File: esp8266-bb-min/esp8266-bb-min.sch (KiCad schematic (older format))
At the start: 22 parts, among them J1 Conn_01x02_Male, J2 Conn_01x04_Male, J3 Conn_01x04_Male, J4 Conn_01x06_Male, J5 Conn_01x04_Male, J6 Conn_01x04_Male, J7 Conn_01x02_Male, U1 LP38693MP-3.3, U2 ESP-12F

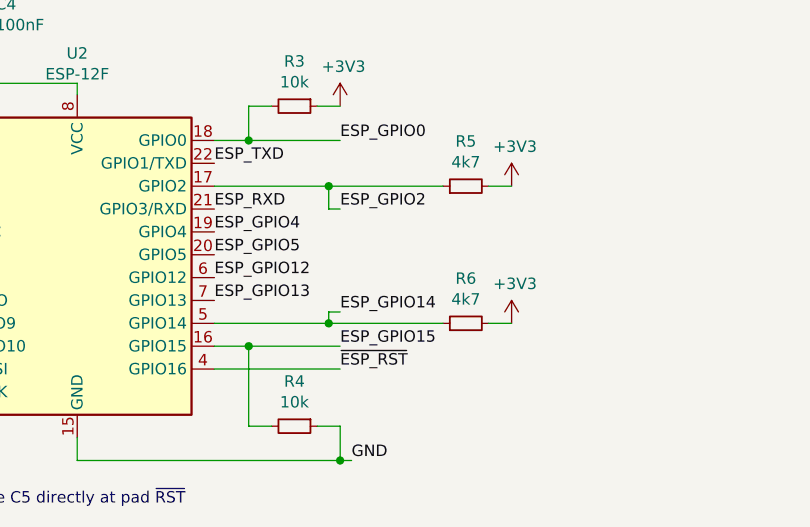
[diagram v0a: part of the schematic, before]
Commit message: sch: added pullups for I2C
Signed-off-by: Dominik Laton <dominik.laton@web.de>
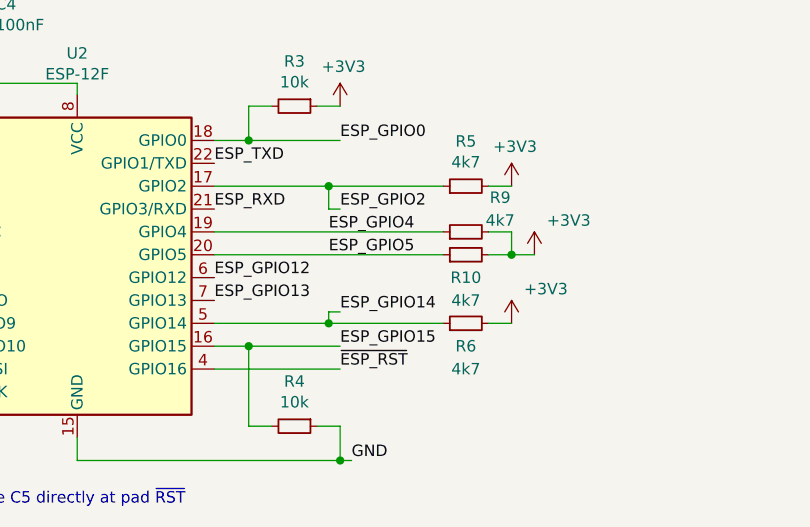
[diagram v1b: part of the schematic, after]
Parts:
- added R10, R9: 4k7, Resistor_SMD:R_0805_2012Metric_Pad1.20x1.40mm_HandSolder, symbol Device:R_Small
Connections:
- net +3V3: now also R10.2, R9.2
- net ESP_GPIO4: now also R9.1
- net ESP_GPIO5: now also R10.1
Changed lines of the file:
@@
 Text Label 6000 4550 0    50   ~ 0
 ESP_GPIO2
-Text Label 5450 4650 0    50   ~ 0
+Text Label 5950 4650 0    50   ~ 0
 ESP_GPIO4
-Text Label 5450 4750 0    50   ~ 0
+Text Label 5950 4750 0    50   ~ 0
 ESP_GPIO5
 Text Label 5450 4850 0    50   ~ 0
@@
 U 1 1 5FA4CD19
 P 6550 5050
-F 0 "R6" V 6746 5050 50  0000 C CNN
-F 1 "4k7" V 6655 5050 50  0000 C CNN
+F 0 "R6" V 6450 5050 50  0000 C CNN
+F 1 "4k7" V 6350 5050 50  0000 C CNN
 F 2 "Resistor_SMD:R_0805_2012Metric_Pad1.20x1.40mm_HandSolder" H 6550 5050 50  0001 C CNN
 F 3 "~" H 6550 5050 50  0001 C CNN
@@
 P 6750 5050
 F 0 "#PWR0106" H 6750 4900 50  0001 C CNN
-F 1 "+3V3" H 6765 5223 50  0000 C CNN
+F 1 "+3V3" H 6900 5200 50  0000 C CNN
 F 2 "" H 6750 5050 50  0001 C CNN
 F 3 "" H 6750 5050 50  0001 C CNN
@@
 Wire Wire Line
 	3000 4650 4250 4650
+Wire Wire Line
+	5450 4650 6450 4650
+Wire Wire Line
+	5450 4750 6450 4750
+$Comp
+L Device:R_Small R9
+U 1 1 5FCD3F71
+P 6550 4650
+F 0 "R9" V 6700 4500 50  0000 C CNN
+F 1 "4k7" V 6600 4500 50  0000 C CNN
+F 2 "Resistor_SMD:R_0805_2012Metric_Pad1.20x1.40mm_HandSolder" H 6550 4650 50  0001 C CNN
+F 3 "~" H 6550 4650 50  0001 C CNN
+	1    6550 4650
+	0    -1   -1   0
+$EndComp
+$Comp
+L Device:R_Small R10
+U 1 1 5FCD43EC
+P 6550 4750
+F 0 "R10" V 6450 4750 50  0000 C CNN
+F 1 "4k7" V 6350 4750 50  0000 C CNN
+F 2 "Resistor_SMD:R_0805_2012Metric_Pad1.20x1.40mm_HandSolder" H 6550 4750 50  0001 C CNN
+F 3 "~" H 6550 4750 50  0001 C CNN
+	1    6550 4750
+	0    -1   -1   0
+$EndComp
+Wire Wire Line
+	6650 4650 6750 4650
+Wire Wire Line
+	6650 4750 6750 4750
+Wire Wire Line
+	6750 4750 6750 4650
+Wire Wire Line
+	6750 4750 6850 4750
+Connection ~ 6750 4750
+$Comp
+L power:+3V3 #PWR012
+U 1 1 5FCEA72A
+P 6850 4750
+F 0 "#PWR012" H 6850 4600 50  0001 C CNN
+F 1 "+3V3" H 7000 4900 50  0000 C CNN
+F 2 "" H 6850 4750 50  0001 C CNN
+F 3 "" H 6850 4750 50  0001 C CNN
+	1    6850 4750
+	1    0    0    -1
+$EndComp
 $EndSCHEMATC
